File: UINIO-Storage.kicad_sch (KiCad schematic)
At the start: 23 parts, among them J1 Conn_01x06_Pin, J2 Conn_01x04_Pin, J3 Conn_01x04_Pin, U1 I2C-24-EEPROM-SOIC8, U2 I2C-24-EEPROM-TSSOP8, U3 SPI-25-Flash-SOIC8

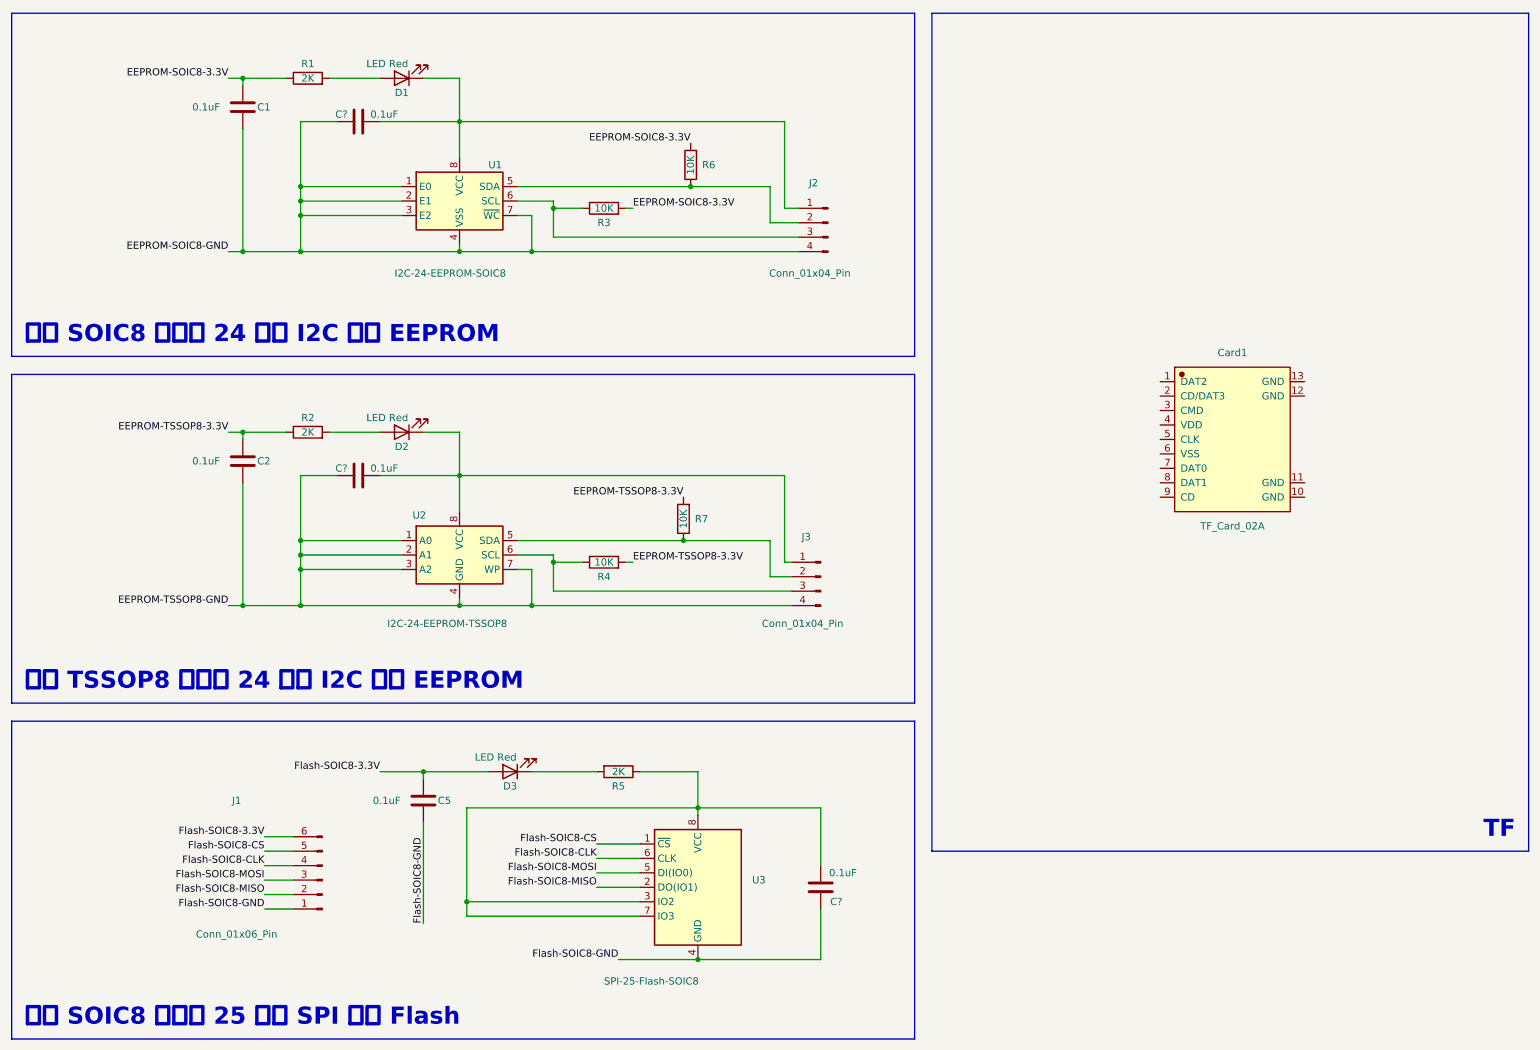
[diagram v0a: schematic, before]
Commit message: Commit IC datasheet.
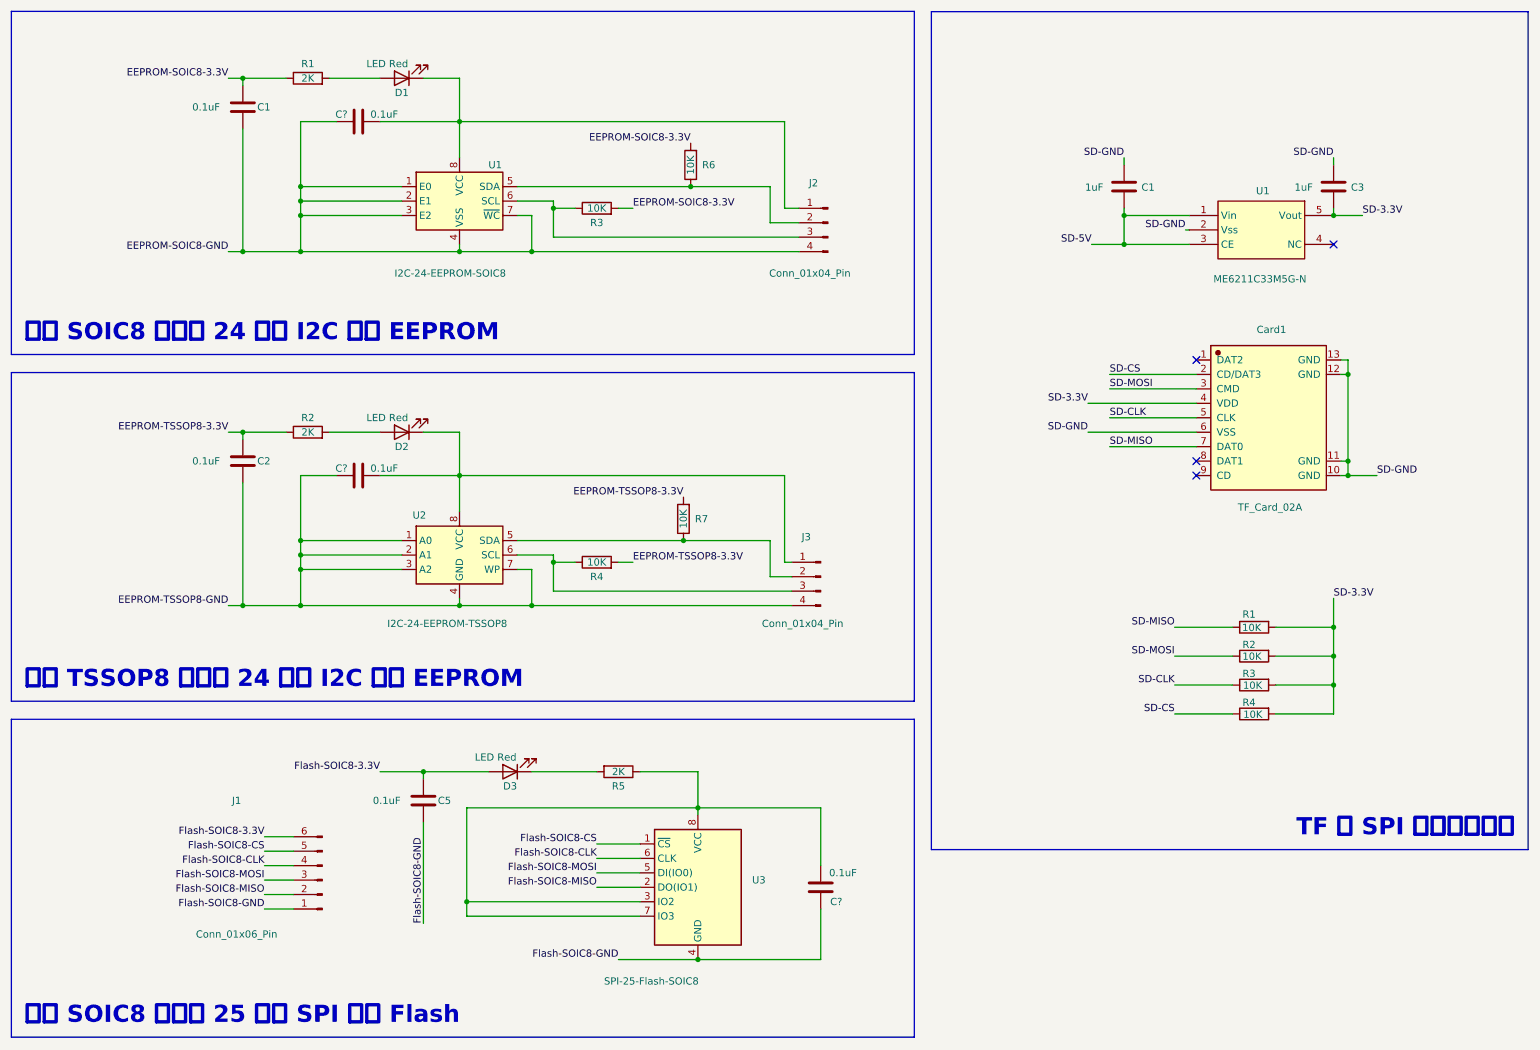
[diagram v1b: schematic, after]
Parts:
- added C1, C3: 1uF, Capacitor_SMD:C_0603_1608Metric, symbol Device:C
- added R1, R2, R3, R4: 10K, Uinio:RES_0402, symbol Uinio:RES_0402
- added U1: ME6211C33M5G-N, Uinio:SOT-23-5_L3.0-W1.7-P0.95-LS2.8-BR, symbol Uinio:ME6211
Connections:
- net SD-GND: now reaches Card1.10 (GND)
- net SD-GND: now also Card1.11 (GND), Card1.12 (GND), Card1.13 (GND), Card1.6 (VSS), C1.1, C3.1, U1.2 (Vss)
- net SD-CS: now reaches Card1.2 (CD/DAT3)
- net SD-CS: now also R4.2
- net SD-MOSI: now reaches Card1.3 (CMD)
- net SD-MOSI: now also R2.2
- net SD-3.3V: now reaches Card1.4 (VDD)
- net SD-3.3V: now also C3.2, R1.1, R2.1, R3.1, R4.1, U1.5 (Vout)
- net SD-CLK: now reaches Card1.5 (CLK)
- net SD-CLK: now also R3.2
- net SD-MISO: now reaches Card1.7 (DAT0)
- net SD-MISO: now also R1.2
- new net SD-5V: C1.2, U1.1 (Vin), U1.3 (CE)
- no-connect marks 0 -> 4
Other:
- moved on the sheet: R3, R4

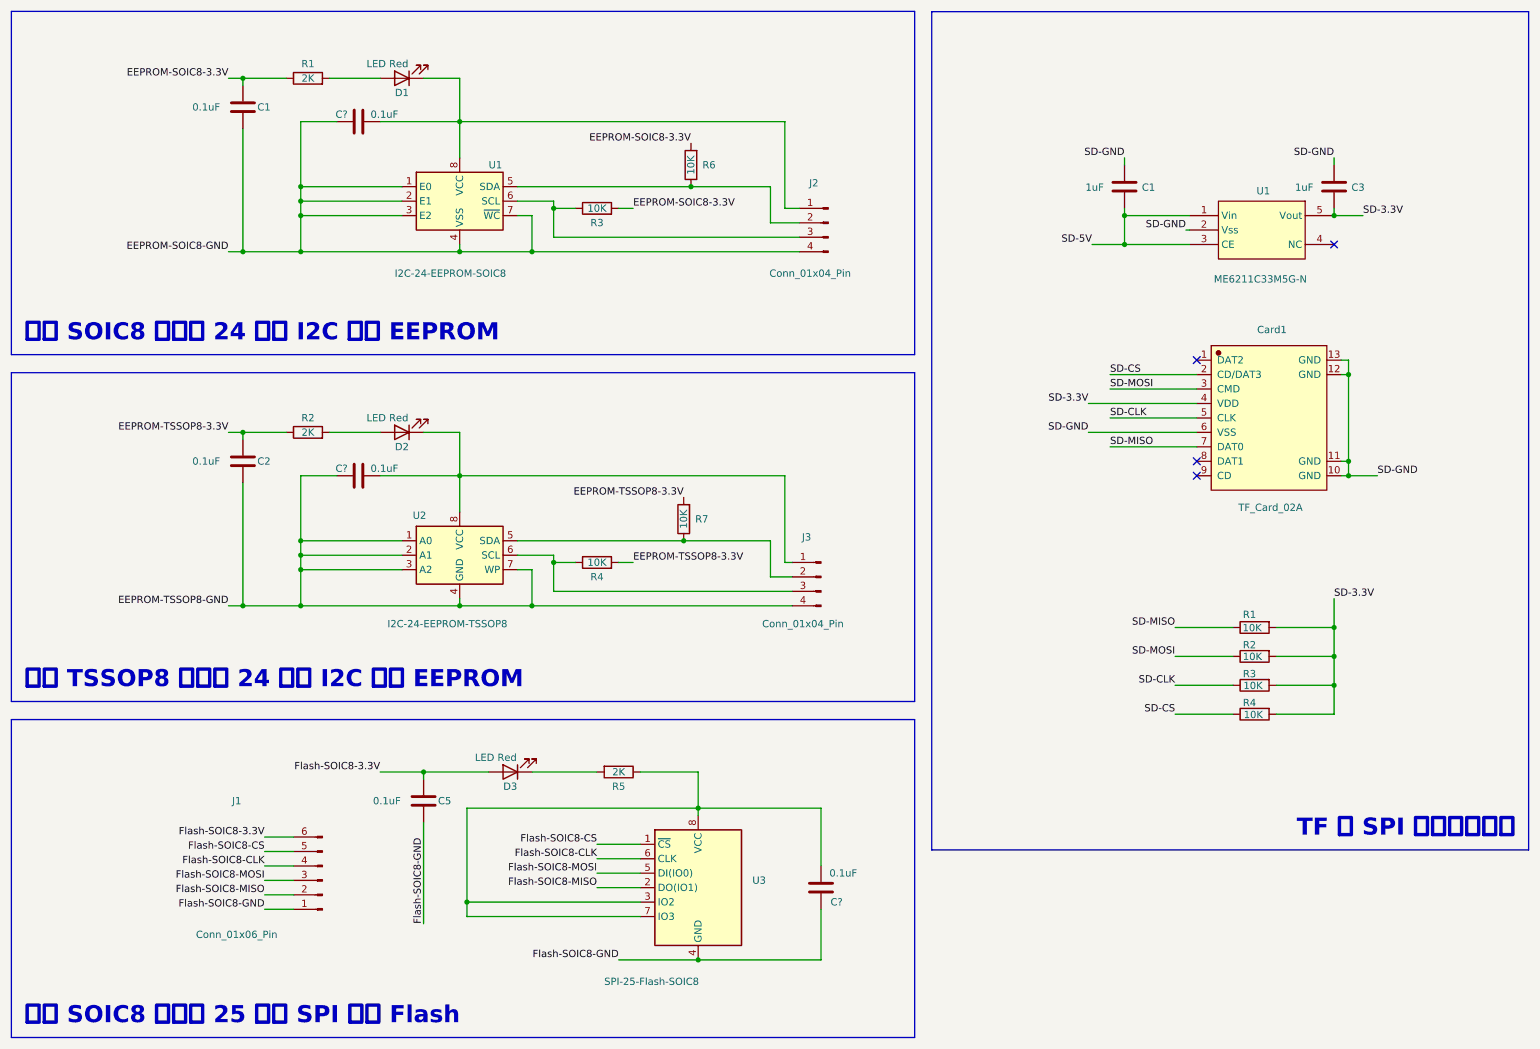
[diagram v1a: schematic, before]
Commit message: Finish schematic diagram.
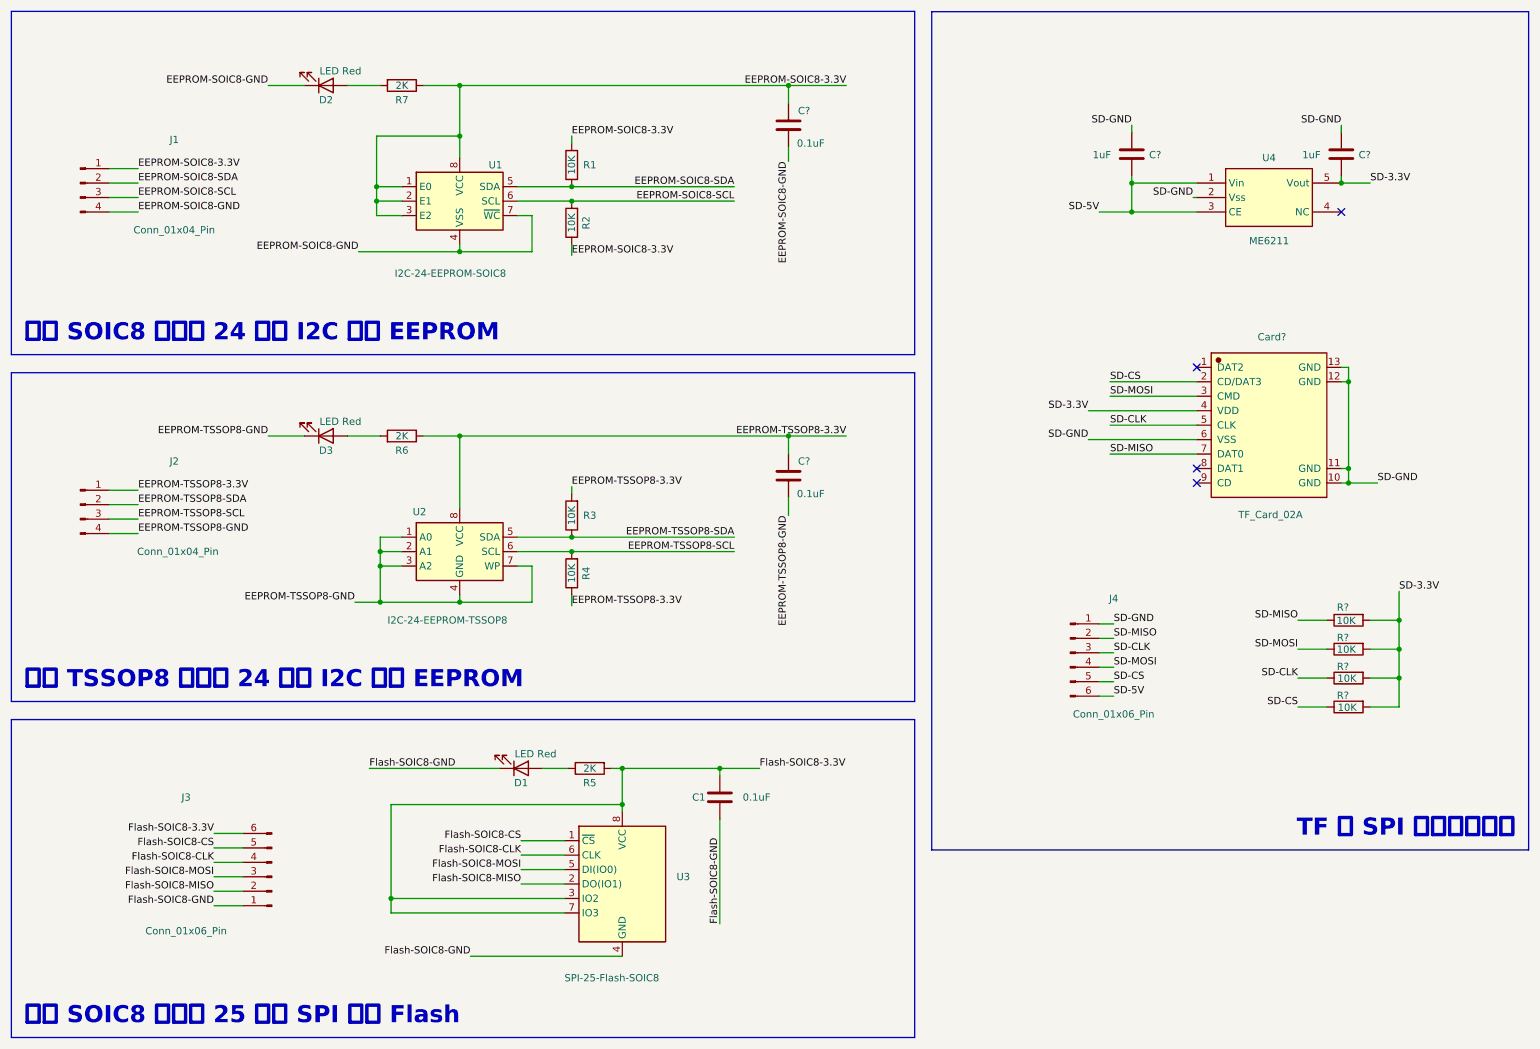
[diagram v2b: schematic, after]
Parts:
- removed C1, C2, C? (x2): 0.1uF, Capacitor_SMD:C_0402_1005Metric, symbol Device:C
- removed D2: LED Red, LED_SMD:LED_0603_1608Metric, symbol Device:LED
- removed J3: Conn_01x04_Pin, Connector_PinHeader_2.54mm:PinHeader_1x04_P2.54mm_Vertical, symbol Connector:Conn_01x04_Pin
- removed R2: 2K, Resistor_SMD:R_0402_1005Metric, symbol Device:R
- removed R7: 10K, Resistor_SMD:R_0402_1005Metric, symbol Device:R
- removed U1: ME6211C33M5G-N, Uinio:SOT-23-5_L3.0-W1.7-P0.95-LS2.8-BR, symbol Uinio:ME6211
- added C?: 0.1uF, Capacitor_SMD:C_0402_1005Metric, symbol Device:C
- added D3: LED Red, LED_SMD:LED_0603_1608Metric, symbol Device:LED
- added J2: Conn_01x04_Pin, Connector_PinHeader_2.54mm:PinHeader_1x04_P2.54mm_Vertical, symbol Connector:Conn_01x04_Pin
- added J4: Conn_01x06_Pin, Connector_PinHeader_2.54mm:PinHeader_1x06_P2.54mm_Vertical, symbol Connector:Conn_01x06_Pin
- added R3: 10K, Resistor_SMD:R_0402_1005Metric, symbol Device:R
- added R6: 2K, Resistor_SMD:R_0402_1005Metric, symbol Device:R
- added U4: ME6211, Uinio:SOT-23-5_L3.0-W1.7-P0.95-LS2.8-BR, symbol Uinio:ME6211
- R?: renamed from R1; footprint Uinio:RES_0402 -> Resistor_SMD:R_0603_1608Metric
- R?: renamed from R4; footprint Uinio:RES_0402 -> Resistor_SMD:R_0603_1608Metric
- R?: renamed from R2; footprint Uinio:RES_0402 -> Resistor_SMD:R_0603_1608Metric
- R?: renamed from R3; footprint Uinio:RES_0402 -> Resistor_SMD:R_0603_1608Metric
- renumbered C5 to C1, C3 to C?, C1 to C?, Card1 to Card?, D3 to D1, D1 to D2, J2 to J1, J1 to J3, R6 to R1, R3 to R2, R1 to R7
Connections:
- net EEPROM-SOIC8-3.3V: now also C?.2, J1.1 (Pin_1), R2.1, U1.1 (E0), U1.2 (E1), U1.3 (E2), U1.8 (VCC); no longer R2.2
- net EEPROM-SOIC8-GND: now also D2.1 (K); no longer U1.1 (E0), U1.2 (E1), U1.3 (E2)
- net EEPROM-TSSOP8-3.3V: now also R4.1, U2.8 (VCC), C?.2, J2.1 (Pin_1), R3.2, R6.1; no longer R4.2
- net EEPROM-TSSOP8-GND: now also C?.1, D3.1 (K), J2.4 (Pin_4)
- net Flash-SOIC8-3.3V: now also R5.2, U3.3 (IO2), U3.7 (IO3), U3.8 (VCC); no longer D1.2 (A)
- net Flash-SOIC8-GND: now also D1.1 (K)
- net SD-3.3V: now also U4.5 (Vout)
- net SD-5V: now also J4.6 (Pin_6), U4.1 (Vin), U4.3 (CE)
- net SD-CLK: now also J4.3 (Pin_3)
- net SD-CS: now also J4.5 (Pin_5)
- net SD-GND: now also J4.1 (Pin_1), U4.2 (Vss)
- net SD-MISO: now also J4.2 (Pin_2)
- net SD-MOSI: now also J4.4 (Pin_4)
- net EEPROM-SOIC8-SDA: now reaches J1.2 (Pin_2), R1.1, U1.5 (SDA)
- net EEPROM-SOIC8-SCL: now reaches J1.3 (Pin_3), U1.6 (SCL)
- net EEPROM-SOIC8-SCL: now also R2.2; no longer R2.1
- net EEPROM-TSSOP8-SDA: now reaches U2.5 (SDA)
- net EEPROM-TSSOP8-SDA: now also J2.2 (Pin_2), R3.1
- net EEPROM-TSSOP8-SCL: now reaches U2.6 (SCL)
- net EEPROM-TSSOP8-SCL: now also R4.2, J2.3 (Pin_3); no longer R4.1
- new net: D1.2 (A), R5.1
- new net: D3.2 (A), R6.2
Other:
- moved on the sheet: C1, C?, Card?, D1, D2, J1, J3, R1, R2, R5, R7, R?

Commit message: Finish schematic diagram.
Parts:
- added D4: LED Red, LED_SMD:LED_0603_1608Metric, symbol Device:LED
- added R12: 2K, Resistor_SMD:R_0603_1608Metric, symbol Device:R
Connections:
- net SD-3.3V: now also R12.1
- net SD-GND: now also D4.1 (K)
- net SD-CLK renamed SD-SCLK
- new net: D4.2 (A), R12.2
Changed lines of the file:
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@@
   (junction (at 250.19 80.01) (diameter 0) (color 0 0 0 0)
+  )
+  (junction (at 254 45.085) (diameter 0) (color 0 0 0 0)
   )
   (junction (at 80.01 112.395) (diameter 0) (color 0 0 0 0)
@@
     (stroke (width 0) (type default))
   )
+  (wire (pts (xy 254 45.085) (xy 254 49.53))
+    (stroke (width 0) (type default))
+  )
   (wire (pts (xy 250.19 80.01) (xy 250.19 95.25))
     (stroke (width 0) (type default))
@@
     (stroke (width 0) (type default))
   )
+  (wire (pts (xy 254 45.085) (xy 261.62 45.085))
+    (stroke (width 0) (type default))
+  )
   (wire (pts (xy 208.915 132.715) (xy 206.375 132.715))
     (stroke (width 0) (type default))
@@
     (stroke (width 0) (type default))
   )
+  (wire (pts (xy 254 70.485) (xy 254 67.31))
+    (stroke (width 0) (type default))
+  )
   (wire (pts (xy 122.555 147.955) (xy 139.7 147.955))
     (stroke (width 0) (type default))
@@
   )
   (wire (pts (xy 104.14 50.8) (xy 106.68 50.8))
+    (stroke (width 0) (type default))
+  )
+  (wire (pts (xy 254 59.69) (xy 254 57.15))
     (stroke (width 0) (type default))
   )
@@
     (effects (font (size 1.27 1.27)) (justify right bottom))
   )
+  (label "SD-GND" (at 254 70.485 0) (fields_autoplaced)
+    (effects (font (size 1.27 1.27)) (justify left bottom))
+  )
   (label "EEPROM-SOIC8-SCL" (at 142.24 48.26 180) (fields_autoplaced)
     (effects (font (size 1.27 1.27)) (justify right bottom))
@@
     (effects (font (size 1.27 1.27)) (justify left bottom))
   )
-  (label "SD-CLK" (at 208.28 87.63 0) (fields_autoplaced)
+  (label "SD-SCLK" (at 208.28 87.63 0) (fields_autoplaced)
     (effects (font (size 1.27 1.27)) (justify left bottom))
   )
@@
     (effects (font (size 1.27 1.27)) (justify left bottom))
   )
-  (label "SD-CLK" (at 208.915 127.635 0) (fields_autoplaced)
+  (label "SD-SCLK" (at 208.915 127.635 0) (fields_autoplaced)
     (effects (font (size 1.27 1.27)) (justify left bottom))
   )
@@
     (effects (font (size 1.27 1.27)) (justify right bottom))
   )
-  (label "SD-3.3V" (at 254 45.085 0) (fields_autoplaced)
+  (label "SD-3.3V" (at 261.62 45.085 0) (fields_autoplaced)
     (effects (font (size 1.27 1.27)) (justify left bottom))
   )
@@
     (effects (font (size 1.27 1.27)) (justify left bottom))
   )
-  (label "SD-CLK" (at 241.3 132.08 180) (fields_autoplaced)
+  (label "SD-SCLK" (at 241.3 132.08 180) (fields_autoplaced)
     (effects (font (size 1.27 1.27)) (justify right bottom))
   )
@@
   (label "Flash-SOIC8-GND" (at 95.885 180.975 180) (fields_autoplaced)
     (effects (font (size 1.27 1.27)) (justify right bottom))
+  )
+  (symbol (lib_id "Device:R") (at 254 53.34 0) (unit 1)
+    (in_bom yes) (on_board yes) (dnp no)
+    (property "Reference" "R12" (at 257.175 53.34 0)
+      (effects (font (size 1.27 1.27)))
+    )
+    (property "Value" "2K" (at 254 53.34 90)
+      (effects (font (size 1.27 1.27)))
+    )
+    (property "Footprint" "Resistor_SMD:R_0603_1608Metric" (at 252.222 53.34 90)
+      (effects (font (size 1.27 1.27)) hide)
+    )
+    (property "Datasheet" "~" (at 254 53.34 0)
+      (effects (font (size 1.27 1.27)) hide)
+    )
+    (pin "1")
+    (pin "2")
+    (instances
+      (project "UINIO-Storage"
+        (path "/c9420995-43a7-497c-95f3-f431f6cd9989"
+          (reference "R12") (unit 1)
+        )
+      )
+      (project "UINIO-USB-Serial"
+        (path "/d8ec999c-704b-44fc-93f3-545dce926477"
+          (reference "R?") (unit 1)
+        )
+      )
+    )
   )
   (symbol (lib_id "Device:R") (at 113.665 41.91 180) (unit 1)
@@
         )
       )
+    )
+  )
+  (symbol (lib_id "Device:LED") (at 254 63.5 270) (mirror x) (unit 1)
+    (in_bom yes) (on_board yes) (dnp no)
+    (property "Reference" "D4" (at 256.54 60.325 90)
+      (effects (font (size 1.27 1.27)))
+    )
+    (property "Value" "LED Red" (at 259.715 64.135 90)
+      (effects (font (size 1.27 1.27)))
+    )
+    (property "Footprint" "LED_SMD:LED_0603_1608Metric" (at 254 63.5 0)
+      (effects (font (size 1.27 1.27)) hide)
+    )
+    (property "Datasheet" "~" (at 254 63.5 0)
+      (effects (font (size 1.27 1.27)) hide)
+    )
+    (pin "2")
+    (pin "1")
+    (instances
+      (project "UINIO-Storage"
+        (path "/c9420995-43a7-497c-95f3-f431f6cd9989"
+          (reference "D4") (unit 1)
+        )
+      )
+      (project "UINIO-USB-Serial"
+        (path "/d8ec999c-704b-44fc-93f3-545dce926477"
+          (reference "D?") (unit 1)
+        )
+      )

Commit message: Commit PCB layout.
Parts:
- added C4: 0.1uF, Capacitor_SMD:C_0402_1005Metric, symbol Device:C
- added D5: LED Red, LED_SMD:LED_0603_1608Metric, symbol Device:LED
- added J5: Conn_01x06_Pin, Connector_PinHeader_2.54mm:PinHeader_1x06_P2.54mm_Vertical, symbol Connector:Conn_01x06_Pin
- added R13: 2K, Resistor_SMD:R_0402_1005Metric, symbol Device:R
- added U5: SPI-25-Flash-WSON8, Package_SON:WSON-8-1EP_6x5mm_P1.27mm_EP3.4x4.3mm, symbol Memory_Flash:W25Q32JVZP
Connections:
- new net: D5.2 (A), R13.1
- new net Flash-WSON8-3.3V: C4.1, J5.6 (Pin_6), R13.2, U5.3 (IO2), U5.7 (IO3), U5.8 (VCC)
- new net Flash-WSON8-CLK: J5.4 (Pin_4), U5.6 (CLK)
- new net Flash-WSON8-CS: J5.5 (Pin_5), U5.1 (~{CS})
- new net Flash-WSON8-GND: C4.2, D5.1 (K), J5.1 (Pin_1), U5.4 (GND), U5.9 (EP)
- new net Flash-WSON8-MISO: J5.2 (Pin_2), U5.2 (DO(IO1))
- new net Flash-WSON8-MOSI: J5.3 (Pin_3), U5.5 (DI(IO0))
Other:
- moved on the sheet: C1, C?, Card?, D1, D2, D3, D4, J1, J2, J3, J4, R1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
